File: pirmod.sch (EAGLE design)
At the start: 12 parts, among them IC1 TLC555CD, K1 22V, K2 LSP10, K3 LSP10

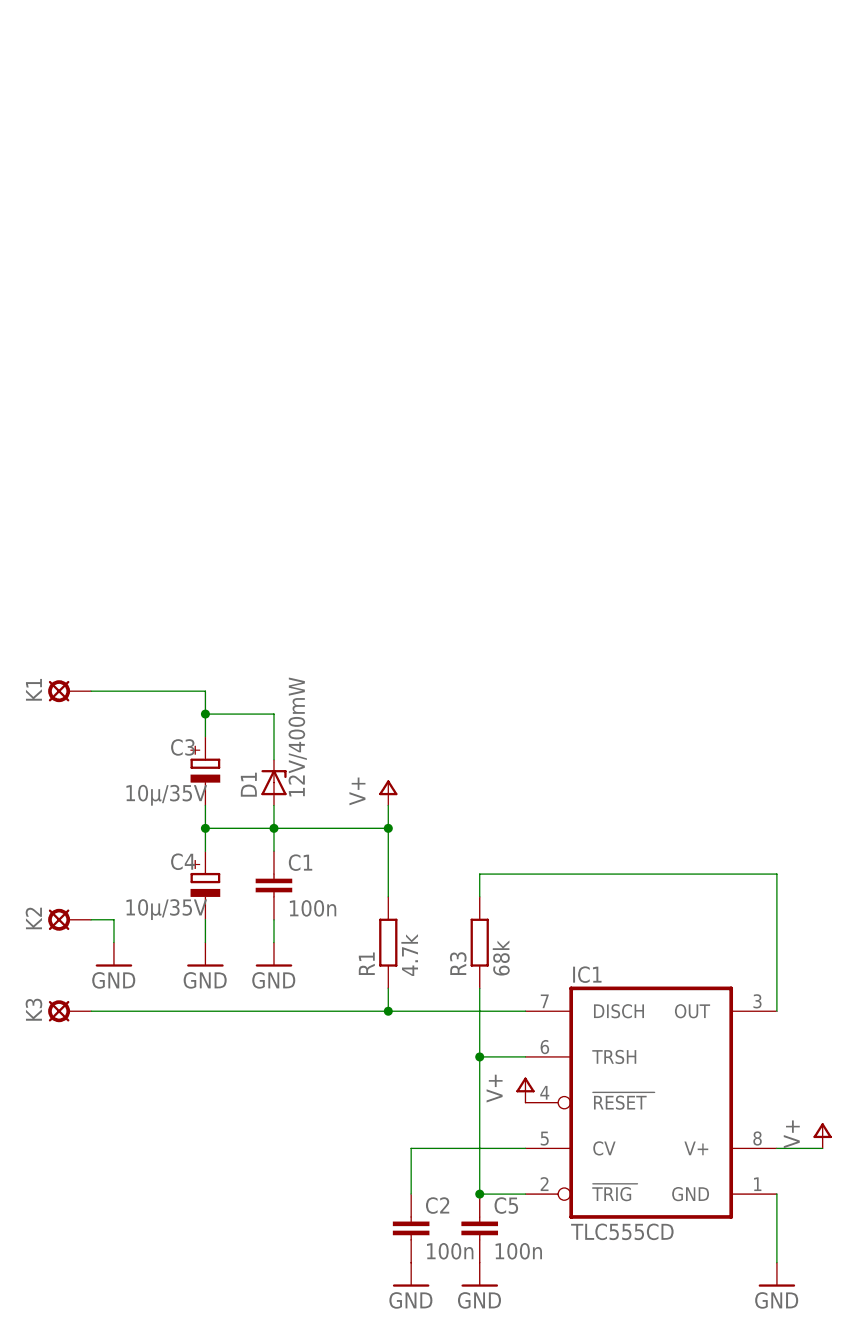
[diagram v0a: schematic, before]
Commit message: Endstufe entfernt
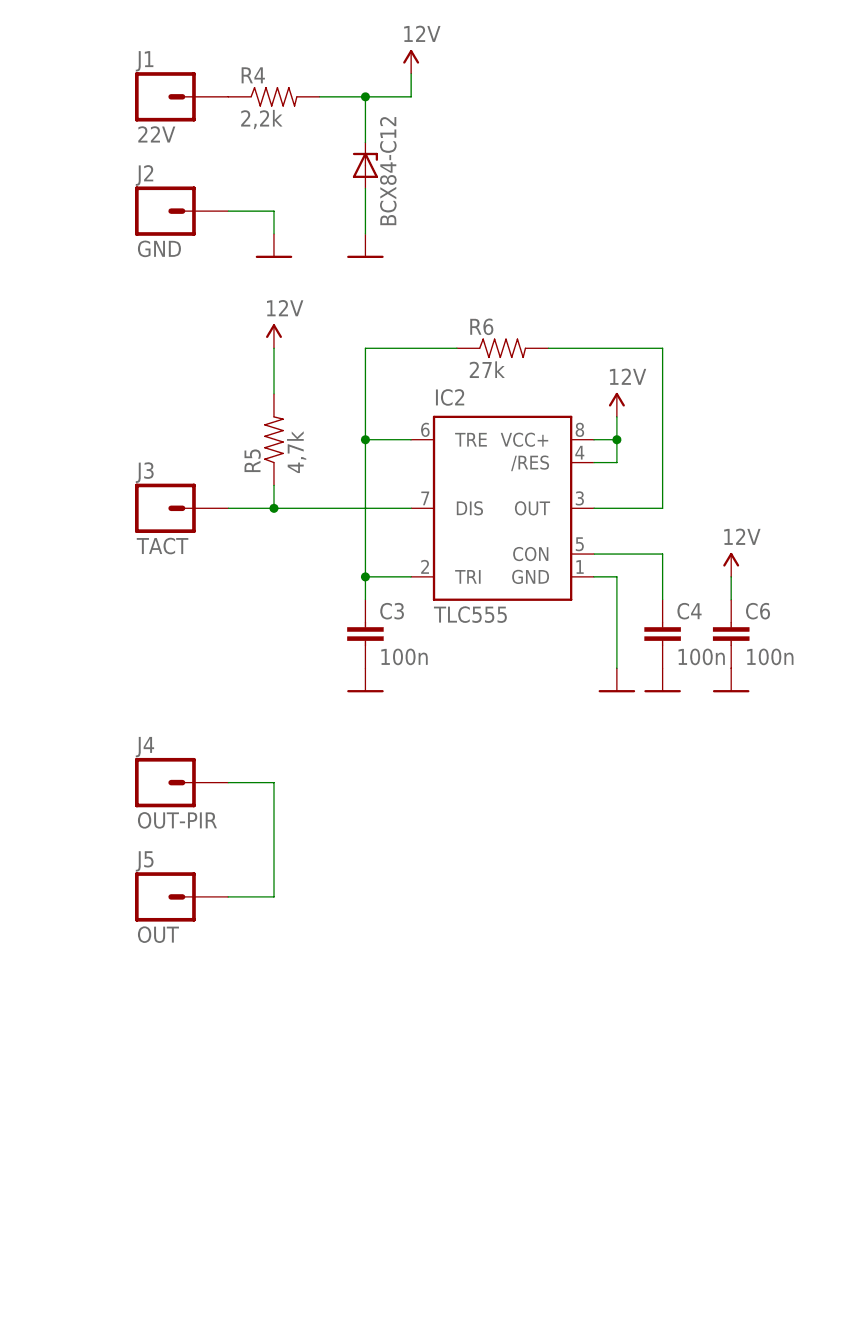
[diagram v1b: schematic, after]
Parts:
- removed C1, C2, C5: 100n, rcl:C-EUC0805K
- removed D1: 12V/400mW, mahiso:ZDIODE
- removed IC1: TLC555CD, mahiso:TLC555CD
- removed K1: 22V, solpad:LSP10
- removed K2, K3: LSP10, solpad:LSP10
- removed R1: 4.7k, rcl:R-EU_M0805
- removed R3: 68k, rcl:R-EU_M0805
- added C6: 100n, SparkFun-Capacitors:CAP0805
- added D2: BCX84-C12, diode:ZENER-DIODESOT23
- added IC2: TLC555, SparkFun-AnalogIC:NE555D
- added J1: 22V, SparkFun-Connectors:M01PTH
- added J2: GND, SparkFun-Connectors:M01SMD-4.5X1.5
- added J3: TACT, SparkFun-Connectors:M01PTH
- added J4: OUT-PIR, SparkFun-Connectors:M01PTH
- added J5: OUT, SparkFun-Connectors:M01PTH
- added R4: 2,2k, SparkFun-Passives:RESISTOR0805-RES
- added R5: 4,7k, SparkFun-Passives:RESISTOR0805-RES
- added R6: 27k, SparkFun-Passives:RESISTOR0805-RES
- C3, C4: value 10µ/35V -> 100n; device rcl:CPOL-EUC -> SparkFun-Capacitors:CAP0805
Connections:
- removed net N$2: C2.1, IC1.CV
- removed net N$6: IC1.OUT, R3.2
- removed net TAKT: IC1.DISCH, K3.MP, R1.1
- removed net V+: C1.1, C3.-, C4.+, D1.A, IC1.RESET, IC1.V+, R1.2
- removed net V+22V: C3.+, D1.C, K1.MP
- new net 12V: C6.1, D2.C, IC2./RES, IC2.VCC+, R4.2, R5.2
- new net N$3: C3.1, IC2.TRE, IC2.TRI, R6.1
- new net N$5: J1.1, R4.1
- new net N$7: C4.1, IC2.CON
- new net N$8: IC2.OUT, R6.2
- new net N$9: IC2.DIS, J3.1, R5.1
- net GND: now also C3.2, C4.2, C6.2, D2.A, IC2.GND, J2.1; no longer C1.2, C2.2, C4.-, C5.2, IC1.GND, K2.MP
- net N$1: now also J4.1, J5.1; no longer C5.1, IC1.TRIG, IC1.TRSH, R3.1

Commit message: V1
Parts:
- D2: device diode:ZENER-DIODESOT23 -> SparkFun-DiscreteSemi:DIODE-ZENER12V
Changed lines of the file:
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@@
 <part name="R5" library="SparkFun-Passives" deviceset="RESISTOR" device="0805-RES" value="4,7k"/>
 <part name="R6" library="SparkFun-Passives" deviceset="RESISTOR" device="0805-RES" value="27k"/>
-<part name="D2" library="diode" deviceset="ZENER-DIODE" device="SOT23" value="BCX84-C12"/>
+<part name="D2" library="SparkFun-DiscreteSemi" deviceset="DIODE-ZENER" device="12V" value="BCX84-C12"/>
 <part name="GND10" library="SparkFun-Aesthetics" deviceset="GND" device="" value=""/>
 <part name="GND11" library="SparkFun-Aesthetics" deviceset="GND" device="" value=""/>

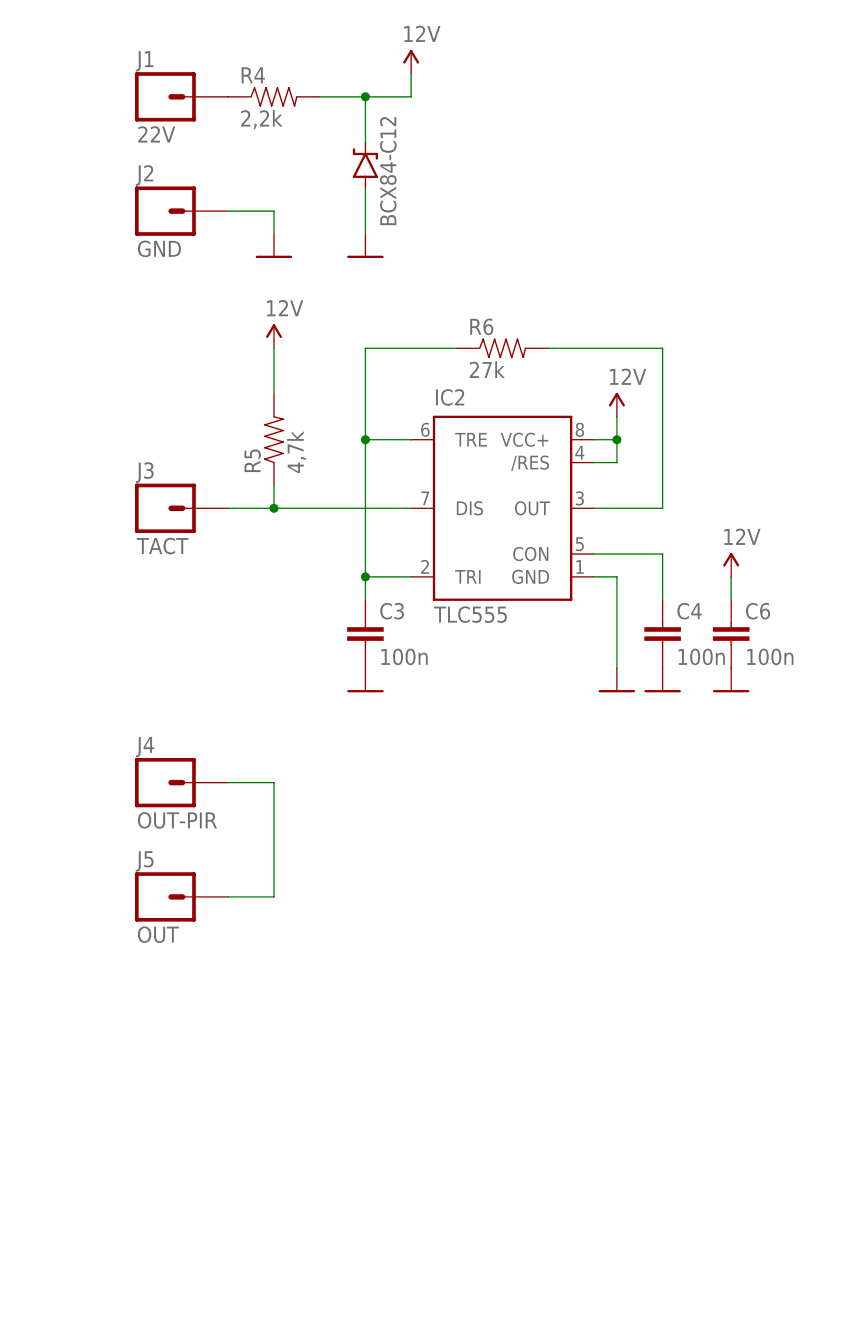
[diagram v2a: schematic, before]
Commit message: Bauteilnummerierung geändert.
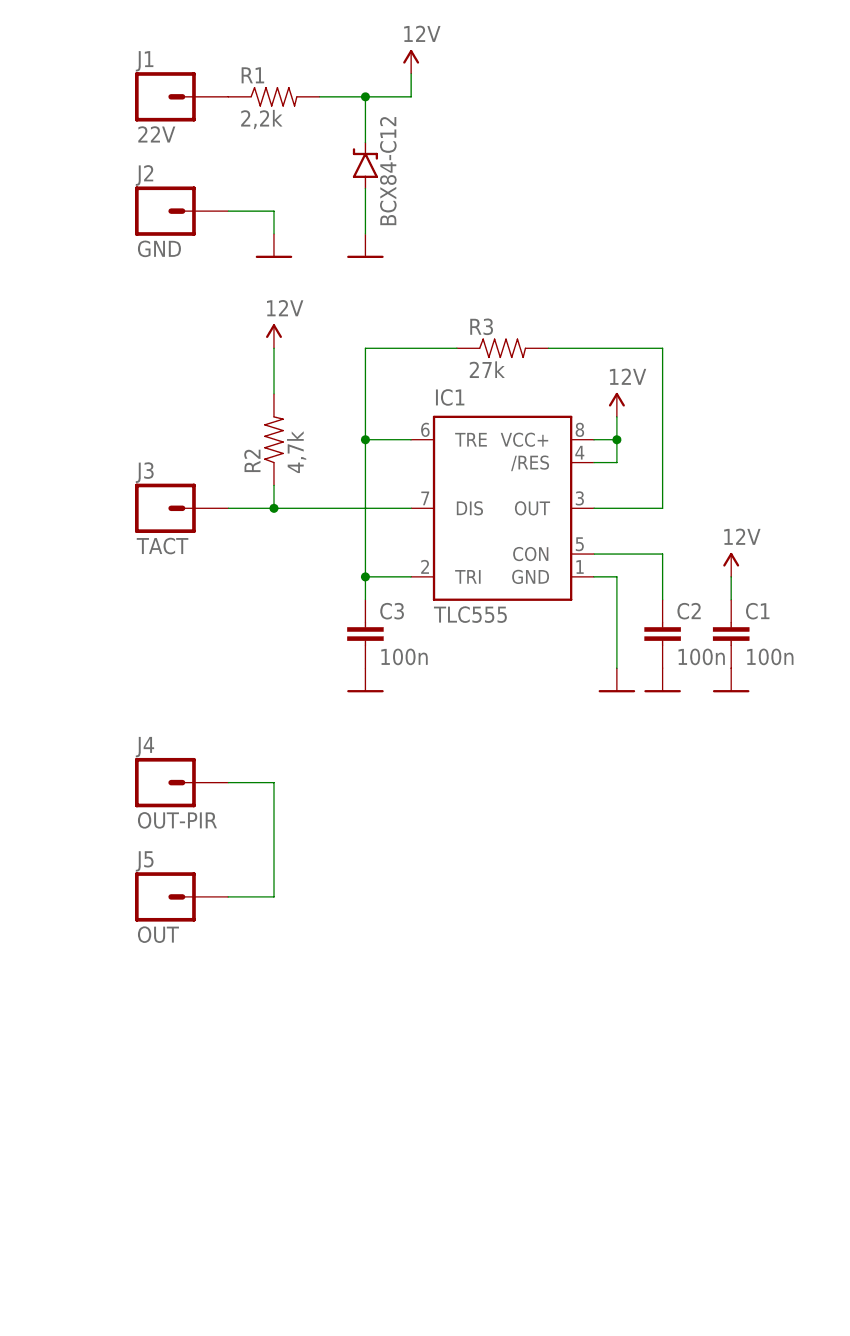
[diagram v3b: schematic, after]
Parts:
- renumbered C4 to C2, C6 to C1, D2 to D1, IC2 to IC1, R4 to R1, R5 to R2, R6 to R3
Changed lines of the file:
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@@
 </classes>
 <parts>
-<part name="IC2" library="SparkFun-AnalogIC" deviceset="NE555" device="D" value="TLC555"/>
+<part name="IC1" library="SparkFun-AnalogIC" deviceset="NE555" device="D" value="TLC555"/>
 <part name="GND6" library="SparkFun-Aesthetics" deviceset="GND" device="" value=""/>
 <part name="GND8" library="SparkFun-Aesthetics" deviceset="GND" device="" value=""/>
 <part name="GND9" library="SparkFun-Aesthetics" deviceset="GND" device="" value=""/>
 <part name="C3" library="SparkFun-Capacitors" deviceset="CAP" device="0805" value="100n"/>
-<part name="C4" library="SparkFun-Capacitors" deviceset="CAP" device="0805" value="100n"/>
-<part name="C6" library="SparkFun-Capacitors" deviceset="CAP" device="0805" value="100n"/>
-<part name="R4" library="SparkFun-Passives" deviceset="RESISTOR" device="0805-RES" value="2,2k"/>
-<part name="R5" library="SparkFun-Passives" deviceset="RESISTOR" device="0805-RES" value="4,7k"/>
-<part name="R6" library="SparkFun-Passives" deviceset="RESISTOR" device="0805-RES" value="27k"/>
-<part name="D2" library="SparkFun-DiscreteSemi" deviceset="DIODE-ZENER" device="12V" value="BCX84-C12"/>
+<part name="C2" library="SparkFun-Capacitors" deviceset="CAP" device="0805" value="100n"/>
+<part name="C1" library="SparkFun-Capacitors" deviceset="CAP" device="0805" value="100n"/>
+<part name="R1" library="SparkFun-Passives" deviceset="RESISTOR" device="0805-RES" value="2,2k"/>
+<part name="R2" library="SparkFun-Passives" deviceset="RESISTOR" device="0805-RES" value="4,7k"/>
+<part name="R3" library="SparkFun-Passives" deviceset="RESISTOR" device="0805-RES" value="27k"/>
+<part name="D1" library="SparkFun-DiscreteSemi" deviceset="DIODE-ZENER" device="12V" value="BCX84-C12"/>
 <part name="GND10" library="SparkFun-Aesthetics" deviceset="GND" device="" value=""/>
 <part name="GND11" library="SparkFun-Aesthetics" deviceset="GND" device="" value=""/>
@@
 </plain>
 <instances>
-<instance part="IC2" gate="G$1" x="71.12" y="104.14"/>
+<instance part="IC1" gate="G$1" x="71.12" y="104.14"/>
 <instance part="GND6" gate="1" x="55.88" y="83.82"/>
 <instance part="GND8" gate="1" x="83.82" y="83.82"/>
 <instance part="GND9" gate="1" x="88.9" y="83.82"/>
 <instance part="C3" gate="G$1" x="55.88" y="88.9"/>
-<instance part="C4" gate="G$1" x="88.9" y="88.9"/>
-<instance part="C6" gate="G$1" x="96.52" y="88.9"/>
-<instance part="R4" gate="G$1" x="45.72" y="149.86"/>
-<instance part="R5" gate="G$1" x="45.72" y="111.76" rot="R90"/>
-<instance part="R6" gate="G$1" x="71.12" y="121.92"/>
-<instance part="D2" gate="G$1" x="55.88" y="142.24" smashed="yes" rot="R90">
+<instance part="C2" gate="G$1" x="88.9" y="88.9"/>
+<instance part="C1" gate="G$1" x="96.52" y="88.9"/>
+<instance part="R1" gate="G$1" x="45.72" y="149.86"/>
+<instance part="R2" gate="G$1" x="45.72" y="111.76" rot="R90"/>
+<instance part="R3" gate="G$1" x="71.12" y="121.92"/>
+<instance part="D1" gate="G$1" x="55.88" y="142.24" smashed="yes" rot="R90">
 <attribute name="VALUE" x="59.309" y="135.382" size="1.778" layer="96" rot="R90"/>
 </instance>
@@
 <net name="GND" class="0">
 <segment>
-<pinref part="C4" gate="G$1" pin="2"/>
+<pinref part="C2" gate="G$1" pin="2"/>
 <pinref part="GND9" gate="1" pin="GND"/>
 </segment>
@@
 </segment>
 <segment>
-<pinref part="IC2" gate="G$1" pin="GND"/>
+<pinref part="IC1" gate="G$1" pin="GND"/>
 <pinref part="GND8" gate="1" pin="GND"/>
 <wire x1="81.28" y1="96.52" x2="83.82" y2="96.52" width="0.1524" layer="91"/>
@@
 </segment>
 <segment>
-<pinref part="C6" gate="G$1" pin="2"/>
+<pinref part="C1" gate="G$1" pin="2"/>
 <pinref part="GND11" gate="1" pin="GND"/>
 </segment>
 <segment>
-<pinref part="D2" gate="G$1" pin="A"/>
+<pinref part="D1" gate="G$1" pin="A"/>
 <pinref part="GND10" gate="1" pin="GND"/>
 <wire x1="55.88" y1="139.7" x2="55.88" y2="134.62" width="0.1524" layer="91"/>
@@
 <net name="N$3" class="0">
 <segment>
-<pinref part="IC2" gate="G$1" pin="TRE"/>
+<pinref part="IC1" gate="G$1" pin="TRE"/>
 <wire x1="60.96" y1="111.76" x2="55.88" y2="111.76" width="0.1524" layer="91"/>
 <wire x1="55.88" y1="111.76" x2="55.88" y2="96.52" width="0.1524" layer="91"/>
-<pinref part="IC2" gate="G$1" pin="TRI"/>
+<pinref part="IC1" gate="G$1" pin="TRI"/>
 <wire x1="55.88" y1="96.52" x2="60.96" y2="96.52" width="0.1524" layer="91"/>
 <pinref part="C3" gate="G$1" pin="1"/>
 <wire x1="55.88" y1="96.52" x2="55.88" y2="93.98" width="0.1524" layer="91"/>
 <junction x="55.88" y="96.52"/>
-<pinref part="R6" gate="G$1" pin="1"/>
+<pinref part="R3" gate="G$1" pin="1"/>
 <wire x1="66.04" y1="121.92" x2="55.88" y2="121.92" width="0.1524" layer="91"/>
 <wire x1="55.88" y1="121.92" x2="55.88" y2="111.76" width="0.1524" layer="91"/>
@@
 <net name="N$7" class="0">
 <segment>
-<pinref part="IC2" gate="G$1" pin="CON"/>
-<pinref part="C4" gate="G$1" pin="1"/>
+<pinref part="IC1" gate="G$1" pin="CON"/>
+<pinref part="C2" gate="G$1" pin="1"/>
 <wire x1="81.28" y1="99.06" x2="88.9" y2="99.06" width="0.1524" layer="91"/>
 <wire x1="88.9" y1="99.06" x2="88.9" y2="93.98" width="0.1524" layer="91"/>
@@
 <net name="N$8" class="0">
 <segment>
-<pinref part="R6" gate="G$1" pin="2"/>
+<pinref part="R3" gate="G$1" pin="2"/>
 <wire x1="76.2" y1="121.92" x2="88.9" y2="121.92" width="0.1524" layer="91"/>
 <wire x1="88.9" y1="121.92" x2="88.9" y2="104.14" width="0.1524" layer="91"/>
-<pinref part="IC2" gate="G$1" pin="OUT"/>
+<pinref part="IC1" gate="G$1" pin="OUT"/>
 <wire x1="88.9" y1="104.14" x2="81.28" y2="104.14" width="0.1524" layer="91"/>
 </segment>
@@
 <net name="N$9" class="0">
 <segment>
-<pinref part="IC2" gate="G$1" pin="DIS"/>
+<pinref part="IC1" gate="G$1" pin="DIS"/>
 <wire x1="60.96" y1="104.14" x2="45.72" y2="104.14" width="0.1524" layer="91"/>
-<pinref part="R5" gate="G$1" pin="1"/>
+<pinref part="R2" gate="G$1" pin="1"/>
 <wire x1="45.72" y1="104.14" x2="45.72" y2="106.68" width="0.1524" layer="91"/>
 <pinref part="J3" gate="G$1" pin="1"/>
@@
 <pinref part="SUPPLY3" gate="G$1" pin="12V"/>
 <wire x1="60.96" y1="152.4" x2="60.96" y2="149.86" width="0.1524" layer="91"/>
-<pinref part="R4" gate="G$1" pin="2"/>
-<pinref part="D2" gate="G$1" pin="C"/>
+<pinref part="R1" gate="G$1" pin="2"/>
+<pinref part="D1" gate="G$1" pin="C"/>
 <wire x1="50.8" y1="149.86" x2="55.88" y2="149.86" width="0.1524" layer="91"/>
 <wire x1="55.88" y1="149.86" x2="55.88" y2="144.78" width="0.1524" layer="91"/>
@@
 </segment>
 <segment>
-<pinref part="R5" gate="G$1" pin="2"/>
+<pinref part="R2" gate="G$1" pin="2"/>
 <pinref part="SUPPLY4" gate="G$1" pin="12V"/>
 <wire x1="45.72" y1="116.84" x2="45.72" y2="121.92" width="0.1524" layer="91"/>
 </segment>
 <segment>
-<pinref part="C6" gate="G$1" pin="1"/>
+<pinref part="C1" gate="G$1" pin="1"/>
 <pinref part="SUPPLY2" gate="G$1" pin="12V"/>
 <wire x1="96.52" y1="93.98" x2="96.52" y2="96.52" width="0.1524" layer="91"/>
 </segment>
 <segment>
-<pinref part="IC2" gate="G$1" pin="/RES"/>
+<pinref part="IC1" gate="G$1" pin="/RES"/>
 <wire x1="81.28" y1="109.22" x2="83.82" y2="109.22" width="0.1524" layer="91"/>
 <wire x1="83.82" y1="109.22" x2="83.82" y2="111.76" width="0.1524" layer="91"/>
-<pinref part="IC2" gate="G$1" pin="VCC+"/>
+<pinref part="IC1" gate="G$1" pin="VCC+"/>
 <wire x1="83.82" y1="111.76" x2="81.28" y2="111.76" width="0.1524" layer="91"/>
 <pinref part="SUPPLY1" gate="G$1" pin="12V"/>
@@
 <net name="N$5" class="0">
 <segment>
-<pinref part="R4" gate="G$1" pin="1"/>
+<pinref part="R1" gate="G$1" pin="1"/>
 <pinref part="J1" gate="G$1" pin="1"/>
 </segment>
